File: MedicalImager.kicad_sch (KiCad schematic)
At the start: 0 parts

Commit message: finished SOM 5V power, migrated altium stuff, finished pin study, added USB PHY (revise HS capability)
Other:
- added sheet Interface (Interface.kicad_sch)
- note added: "TODO: - Complete power circuit (one instance of 4A & 1A modules) - Set up power sequencing stuff - Complete the AD8285's part (duplicated in all replicas) - Figure out power requirements (which banks, USB?, etc.) - Link peripherals in K26 to components - Set up circuit protection measures - Add an SD card (if not found on SOM)"
- note removed: "TODO: - Complete pinout stidy of k26 - Migrate progress in altium to here (TX dcaps)"
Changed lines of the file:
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@@
 	(generator_version "10.0")
 	(paper "A4")
-	(text "TODO:\n- Complete pinout stidy of k26\n- Migrate progress in altium to here (TX dcaps)"
+	(text "TODO:\n- Complete power circuit (one instance of 4A & 1A modules)\n- Set up power sequencing stuff\n- Complete the AD8285's part (duplicated in all replicas)\n- Figure out power requirements (which banks, USB?, etc.)\n- Link peripherals in K26 to components\n- Set up circuit protection measures\n- Add an SD card (if not found on SOM)"
 		(exclude_from_sim no)
-		(at 140.716 142.24 0)
+		(at 30.988 149.352 0)
 		(effects
 			(font
@@
 				(bold yes)
 			)
+			(justify left)
 		)
+	)
+	(sheet
+		(at 203.2 88.9)
+		(size 25.4 25.4)
+		(exclude_from_sim no)
+		(in_bom yes)
+		(on_board yes)
+		(dnp no)
+		(fields_autoplaced yes)
+		(stroke
+			(width 0.1524)
+			(type solid)
+		)
+		(fill
+			(color 0 0 0 0)
+		)
+		(property "Sheetname" "Interface"
+			(at 203.2 88.1884 0)
+			(show_name no)
+			(do_not_autoplace no)
+			(effects
+				(font
+					(size 1.27 1.27)
+				)
+				(justify left bottom)
+			)
+		)
+		(property "Sheetfile" "Interface.kicad_sch"
+			(at 203.2 114.8846 0)
+			(show_name no)
+			(do_not_autoplace no)
+			(effects
+				(font
+					(size 1.27 1.27)
+				)
+				(justify left top)
+			)
+		)
+		(instances
+			(project "MedicalImager"
+				(path "/99848109-7be9-4113-bc9c-faf6c2acfe0b"
+					(page "10")
+				)
+			)
+		)

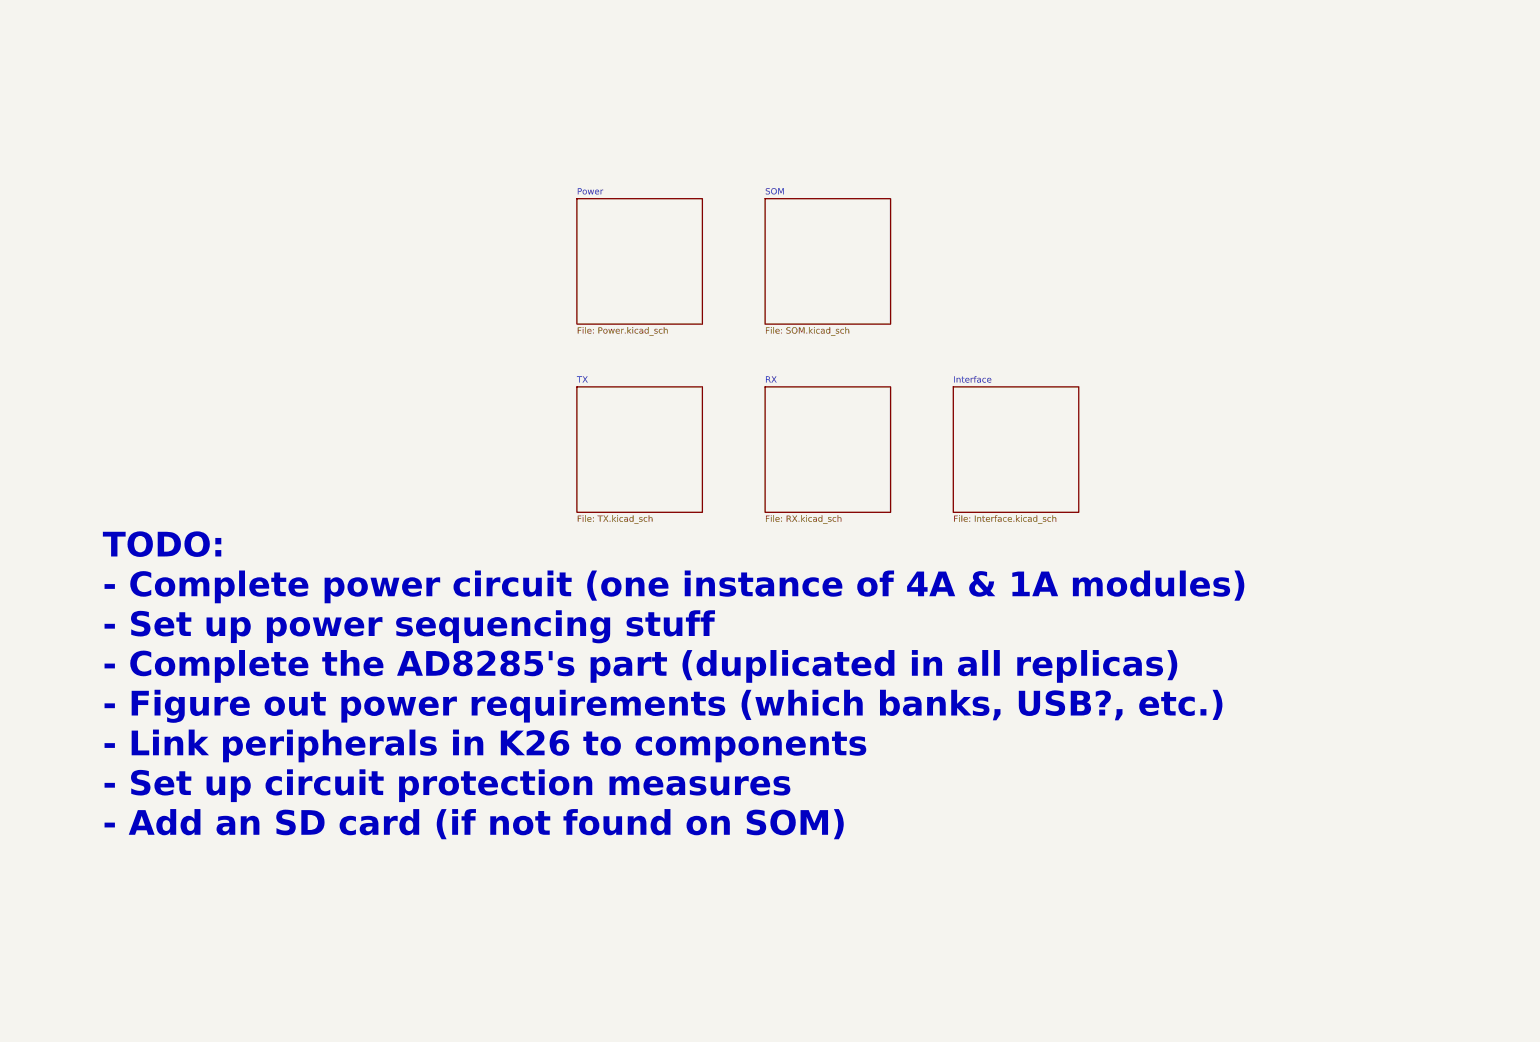
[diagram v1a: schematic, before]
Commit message: finished HV rails (revise, ai), added LDO instances, ready to bind & supply
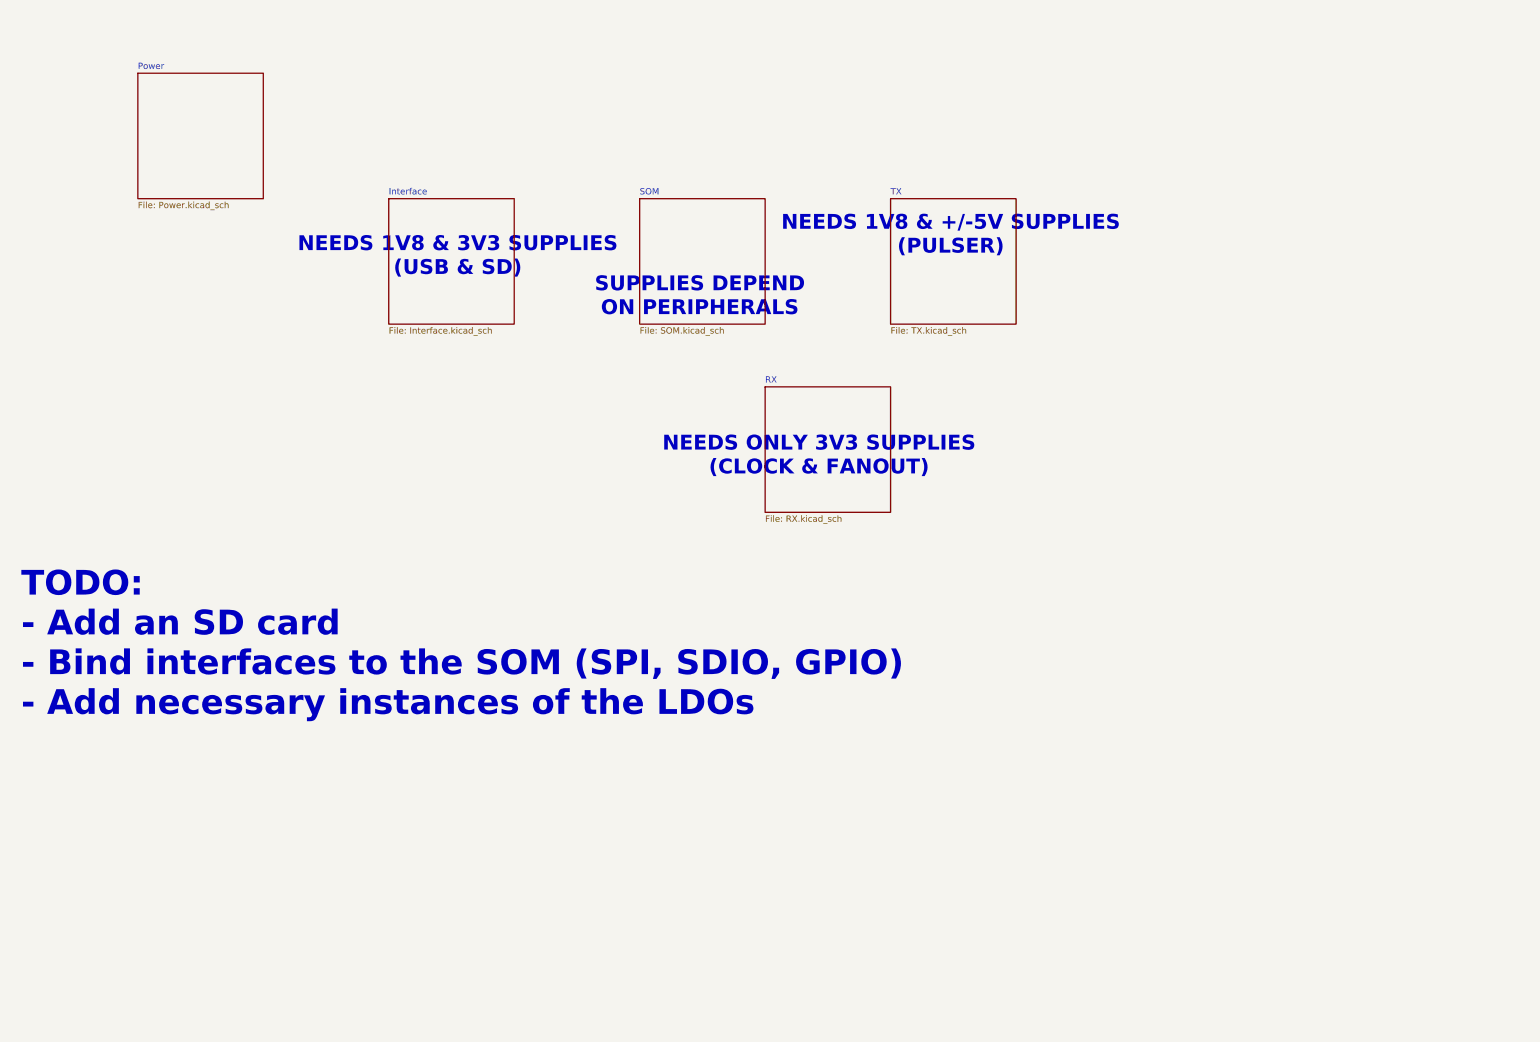
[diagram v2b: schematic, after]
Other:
- note added: "NEEDS 1V8 & +/-5V SUPPLIES (PULSER)"
- note added: "NEEDS 1V8 & 3V3 SUPPLIES (USB & SD)"
- note added: "NEEDS ONLY 3V3 SUPPLIES (CLOCK & FANOUT)"
- note added: "SUPPLIES DEPEND ON PERIPHERALS"
- note added: "TODO: - Add an SD card - Bind interfaces to the SOM (SPI, SDIO, GPIO) - Add necessary instances of the LDOs"
- note removed: "TODO: - Complete power circuit (one instance of 4A & 1A modules) - Set up power sequencing stuff - Complete the AD8285's part (duplicated in all replicas) - Figure out power requirements (which banks, USB?, etc.) - Link peripherals in K26 to components - Set up circuit protection measures - Add an SD card (if not found on SOM)"
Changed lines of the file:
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@@
 	(generator_version "10.0")
 	(paper "A4")
-	(text "TODO:\n- Complete power circuit (one instance of 4A & 1A modules)\n- Set up power sequencing stuff\n- Complete the AD8285's part (duplicated in all replicas)\n- Figure out power requirements (which banks, USB?, etc.)\n- Link peripherals in K26 to components\n- Set up circuit protection measures\n- Add an SD card (if not found on SOM)"
-		(exclude_from_sim no)
-		(at 30.988 149.352 0)
+	(text "TODO:\n- Add an SD card\n- Bind interfaces to the SOM (SPI, SDIO, GPIO)\n- Add necessary instances of the LDOs"
+		(exclude_from_sim no)
+		(at 14.478 140.97 0)
 		(effects
 			(font
@@
 		)
 	)
-	(sheet
-		(at 203.2 88.9)
+	(text "NEEDS 1V8 & +/-5V SUPPLIES\n(PULSER)"
+		(exclude_from_sim no)
+		(at 202.692 58.166 0)
+		(effects
+			(font
+				(size 3 3)
+				(thickness 0.6)
+				(bold yes)
+			)
+		)
+	)
+	(text "SUPPLIES DEPEND\nON PERIPHERALS"
+		(exclude_from_sim no)
+		(at 151.892 70.612 0)
+		(effects
+			(font
+				(size 3 3)
+				(thickness 0.6)
+				(bold yes)
+			)
+		)
+	)
+	(text "NEEDS ONLY 3V3 SUPPLIES\n(CLOCK & FANOUT)"
+		(exclude_from_sim no)
+		(at 176.022 102.87 0)
+		(effects
+			(font
+				(size 3 3)
+				(thickness 0.6)
+				(bold yes)
+			)
+		)
+	)
+	(text "NEEDS 1V8 & 3V3 SUPPLIES\n(USB & SD)"
+		(exclude_from_sim no)
+		(at 102.87 62.484 0)
+		(effects
+			(font
+				(size 3 3)
+				(thickness 0.6)
+				(bold yes)
+			)
+		)
+	)
+	(sheet
+		(at 88.9 50.8)
 		(size 25.4 25.4)
 		(exclude_from_sim no)
@@
 		)
 		(property "Sheetname" "Interface"
-			(at 203.2 88.1884 0)
+			(at 88.9 50.0884 0)
 			(show_name no)
 			(do_not_autoplace no)
@@
 		)
 		(property "Sheetfile" "Interface.kicad_sch"
-			(at 203.2 114.8846 0)
+			(at 88.9 76.7846 0)
 			(show_name no)
 			(do_not_autoplace no)
@@
 	)
 	(sheet
-		(at 165.1 50.8)
+		(at 139.7 50.8)
 		(size 25.4 25.4)
 		(exclude_from_sim no)
@@
 		)
 		(property "Sheetname" "SOM"
-			(at 165.1 50.0884 0)
+			(at 139.7 50.0884 0)
 			(show_name no)
 			(do_not_autoplace no)
@@
 		)
 		(property "Sheetfile" "SOM.kicad_sch"
-			(at 165.1 76.7846 0)
+			(at 139.7 76.7846 0)
 			(show_name no)
 			(do_not_autoplace no)
@@
 	)
 	(sheet
-		(at 127 88.9)
+		(at 190.5 50.8)
 		(size 25.4 25.4)
 		(exclude_from_sim no)
@@
 		)
 		(property "Sheetname" "TX"
-			(at 127 88.1884 0)
+			(at 190.5 50.0884 0)
 			(show_name no)
 			(do_not_autoplace no)
@@
 		)
 		(property "Sheetfile" "TX.kicad_sch"
-			(at 127 114.8846 0)
+			(at 190.5 76.7846 0)
 			(show_name no)
 			(do_not_autoplace no)
@@
 	)
 	(sheet
-		(at 127 50.8)
+		(at 38.1 25.4)
 		(size 25.4 25.4)
 		(exclude_from_sim no)
@@
 		)
 		(property "Sheetname" "Power"
-			(at 127 50.0884 0)
+			(at 38.1 24.6884 0)
 			(show_name no)
 			(do_not_autoplace no)
@@
 		)
 		(property "Sheetfile" "Power.kicad_sch"
-			(at 127 76.7846 0)
-			(show_name no)
-			(do_not_autoplace no)
+			(at 38.1 51.3846 0)
+			(show_name no)
+			(do_not_autoplace no)

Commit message: added USB (needs revision), fixed medium voltage rail
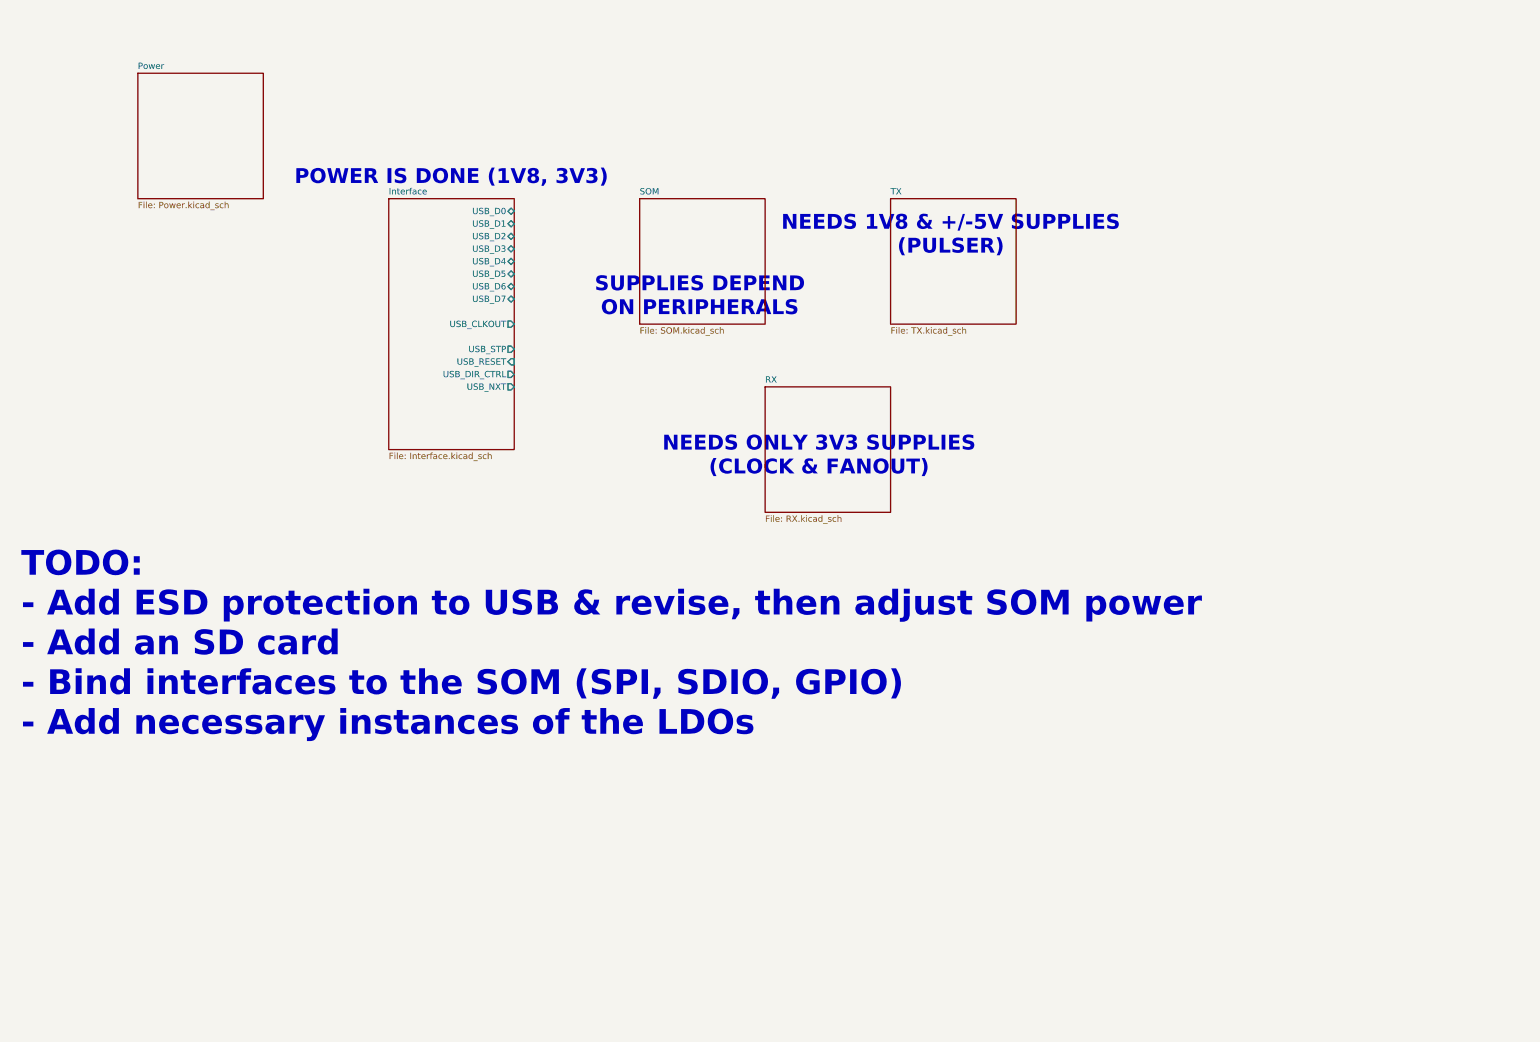
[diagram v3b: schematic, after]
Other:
- sheet Interface ports: added USB_CLKOUT, USB_D0, USB_D1, USB_D2, USB_D3, USB_D4, USB_D5, USB_D6, USB_D7, USB_DIR_CTRL, USB_NXT, USB_RESET, USB_STP; removed none
- note added: "POWER IS DONE (1V8, 3V3)"
- note added: "TODO: - Add ESD protection to USB & revise, then adjust SOM power - Add an SD card - Bind interfaces to the SOM (SPI, SDIO, GPIO) - Add necessary instances of the LDOs"
- note removed: "NEEDS 1V8 & 3V3 SUPPLIES (USB & SD)"
- note removed: "TODO: - Add an SD card - Bind interfaces to the SOM (SPI, SDIO, GPIO) - Add necessary instances of the LDOs"
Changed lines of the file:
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@@
 	(generator_version "10.0")
 	(paper "A4")
-	(text "TODO:\n- Add an SD card\n- Bind interfaces to the SOM (SPI, SDIO, GPIO)\n- Add necessary instances of the LDOs"
+	(text "TODO:\n- Add ESD protection to USB & revise, then adjust SOM power\n- Add an SD card\n- Bind interfaces to the SOM (SPI, SDIO, GPIO)\n- Add necessary instances of the LDOs"
 		(exclude_from_sim no)
 		(at 14.478 140.97 0)
@@
 		)
 	)
+	(text "POWER IS DONE (1V8, 3V3)"
+		(exclude_from_sim no)
+		(at 101.6 46.482 0)
+		(effects
+			(font
+				(size 3 3)
+				(thickness 0.6)
+				(bold yes)
+			)
+		)
+	)
 	(text "NEEDS ONLY 3V3 SUPPLIES\n(CLOCK & FANOUT)"
 		(exclude_from_sim no)
 		(at 176.022 102.87 0)
-		(effects
-			(font
-				(size 3 3)
-				(thickness 0.6)
-				(bold yes)
-			)
-		)
-	)
-	(text "NEEDS 1V8 & 3V3 SUPPLIES\n(USB & SD)"
-		(exclude_from_sim no)
-		(at 102.87 62.484 0)
 		(effects
 			(font
@@
 	(sheet
 		(at 88.9 50.8)
-		(size 25.4 25.4)
+		(size 25.4 50.8)
 		(exclude_from_sim no)
 		(in_bom yes)
@@
 		)
 		(property "Sheetfile" "Interface.kicad_sch"
-			(at 88.9 76.7846 0)
+			(at 88.9 102.1846 0)
 			(show_name no)
 			(do_not_autoplace no)
@@
 			)
 		)
+		(pin "USB_D7" bidirectional
+			(at 114.3 71.12 0)
+			(effects
+				(font
+					(size 1.27 1.27)
+				)
+				(justify right)
+			)
+		)
+		(pin "USB_D0" bidirectional
+			(at 114.3 53.34 0)
+			(effects
+				(font
+					(size 1.27 1.27)
+				)
+				(justify right)
+			)
+		)
+		(pin "USB_CLKOUT" output
+			(at 114.3 76.2 0)
+			(effects
+				(font
+					(size 1.27 1.27)
+				)
+				(justify right)
+			)
+		)
+		(pin "USB_D4" bidirectional
+			(at 114.3 63.5 0)
+			(effects
+				(font
+					(size 1.27 1.27)
+				)
+				(justify right)
+			)
+		)
+		(pin "USB_D3" bidirectional
+			(at 114.3 60.96 0)
+			(effects
+				(font
+					(size 1.27 1.27)
+				)
+				(justify right)
+			)
+		)
+		(pin "USB_D1" bidirectional
+			(at 114.3 55.88 0)
+			(effects
+				(font
+					(size 1.27 1.27)
+				)
+				(justify right)
+			)
+		)
+		(pin "USB_STP" output
+			(at 114.3 81.28 0)
+			(effects
+				(font
+					(size 1.27 1.27)
+				)
+				(justify right)
+			)
+		)
+		(pin "USB_RESET" input
+			(at 114.3 83.82 0)
+			(effects
+				(font
+					(size 1.27 1.27)
+				)
+				(justify right)
+			)
+		)
+		(pin "USB_D6" bidirectional
+			(at 114.3 68.58 0)
+			(effects
+				(font
+					(size 1.27 1.27)
+				)
+				(justify right)
+			)
+		)
+		(pin "USB_DIR_CTRL" output
+			(at 114.3 86.36 0)
+			(effects
+				(font
+					(size 1.27 1.27)
+				)
+				(justify right)
+			)
+		)
+		(pin "USB_NXT" output
+			(at 114.3 88.9 0)
+			(effects
+				(font
+					(size 1.27 1.27)
+				)
+				(justify right)
+			)
+		)
+		(pin "USB_D5" bidirectional
+			(at 114.3 66.04 0)
+			(effects
+				(font
+					(size 1.27 1.27)
+				)
+				(justify right)
+			)
+		)
+		(pin "USB_D2" bidirectional
+			(at 114.3 58.42 0)
+			(effects
+				(font
+					(size 1.27 1.27)
+				)
+				(justify right)
+			)
+		)

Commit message: almost finished, phew! just dd +/- 5v rails, connect the SDIO & power enable pins and figure out the rest of the clocking chain
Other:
- sheet Interface ports: added SD_CLK, SD_CMD, SD_DAT0, SD_DAT1, SD_DAT2, SD_DAT3, SD_DETECT; removed none
- sheet Power ports: added 100V_EN, 50V_EN, AFE1_1V8_EN, AFE1_3V3_EN, AFE2_1V8_EN, AFE2_3V3_EN, AFE3_1V8_EN, AFE3_3V3_EN, AFE4_1V8_EN, AFE4_3V3_EN, CLK_PWR_EN, IM_5V_PG, PULSER_1V8_EN, SOM_5V_PG, SOM_PL_PWR_EN, USB_1V8_EN; removed none
- sheet RX ports: added AFE1_AUX, AFE1_CSn, AFE1_DSYNC, AFE1_MUXA, AFE2_AUX, AFE2_CSn, AFE2_DSYNC, AFE2_MUXA, AFE3_AUX, AFE3_CSn, AFE3_DSYNC, AFE3_MUXA, AFE4_AUX, AFE4_CSn, AFE4_DSYNC, AFE4_MUXA, AFE_OUTPUTS[0..47], AFE_SCLK, AFE_SDIO, SOM_SYNC_CLK_N, SOM_SYNC_CLK_P, TR_OUT[0..15], TX_BF_CLK_N, TX_BF_CLK_P; removed none
- sheet SOM ports: added 100V_EN, 50V_EN, AFE1_1V8_EN, AFE1_3V3_EN, AFE1_AUX, AFE1_CSn, AFE1_DSYNC, AFE1_MUXA, AFE2_1V8_EN, AFE2_3V3_EN, AFE2_AUX, AFE2_CSn, AFE2_DSYNC, AFE2_MUXA, AFE3_1V8_EN, AFE3_3V3_EN, AFE3_AUX, AFE3_CSn, AFE3_DSYNC, AFE3_MUXA, AFE4_1V8_EN, AFE4_3V3_EN, AFE4_AUX, AFE4_CSn, AFE4_DSYNC, AFE4_MUXA, AFE_OUTPUTS[0..47], AFE_SCLK, AFE_SDIO, CLK_PWR_EN, IM_5V_PG, PULSER_1V8_EN, PULSER_BF_SYNC_CLK_N, PULSER_BF_SYNC_CLK_P, PULSER_CRC_ERR, PULSER_RESET, PULSER_SPI_CLK_N, PULSER_SPI_CLK_P, PULSER_SPI_CRC_EN, PULSER_SPI_CS0, PULSER_SPI_CS1, PULSER_SPI_D0_N, PULSER_SPI_D0_P, PULSER_SPI_D1_N, PULSER_SPI_D1_P, PULSER_SPI_MODE, PULSER_SPI_SDOUT, PULSER_SPI_SE_N, PULSER_SPI_SE_P, PULSER_TSHUT, PULSER_TXRX, PULSER_WAKEUP, SD_CLK, SD_CMD, SD_DAT0, SD_DAT1, SD_DAT2, SD_DAT3, SD_DETECT, SOM_5V_PG, SOM_PL_PWR_EN, SOM_PS_PWR_EN, SOM_SYNC_CLK_N, SOM_SYNC_CLK_P, USB_1V8_EN, USB_CLKOUT, USB_D0, USB_D1, USB_D2, USB_D3, USB_D4, USB_D5, USB_D6, USB_D7, USB_DIR_CTRL, USB_NXT, USB_STP; removed none
- sheet TX ports: added PULSER_BF_CLK_N, PULSER_BF_CLK_P, PULSER_BF_SYNC_CLK_N, PULSER_BF_SYNC_CLK_P, PULSER_CRC_ERR, PULSER_OUT[0..15], PULSER_RESET, PULSER_SPI_CLK_N, PULSER_SPI_CLK_P, PULSER_SPI_CRC_EN, PULSER_SPI_CS0, PULSER_SPI_CS1, PULSER_SPI_D0_N, PULSER_SPI_D0_P, PULSER_SPI_D1_N, PULSER_SPI_D1_P, PULSER_SPI_MODE, PULSER_SPI_SDOUT, PULSER_SPI_SE_N, PULSER_SPI_SE_P, PULSER_TSHUT, PULSER_TXRX, PULSER_WAKEUP, TR_OUT[0..15]; removed none
- note added: "NEEDS +/-5V SUPPLIES (PULSER)"
- note added: "TODO: - Complete missing interfaces (SDIO & clocking) - Check un-supplied rails (including -5V)"
- note removed: "NEEDS 1V8 & +/-5V SUPPLIES (PULSER)"
- note removed: "NEEDS ONLY 3V3 SUPPLIES (CLOCK & FANOUT)"
- note removed: "POWER IS DONE (1V8, 3V3)"
- note removed: "TODO: - Add ESD protection to USB & revise, then adjust SOM power - Add an SD card - Bind interfaces to the SOM (SPI, SDIO, GPIO) - Add necessary instances of the LDOs"

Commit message: DONE! hust needs a final revision, checking termination throughout the circuit and verifying the signal chain
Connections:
- no-connect marks 0 -> 1
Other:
- sheet Power ports: added -5V_EN, IM_5V_EN, SD_3V3_EN; removed none
- sheet SOM ports: added -5V_EN, IM_5V_EN, SD_3V3_EN; removed none
- note added: "- FINALIZE CLOCKING CONNECTIONS AND TERMINATION THROUGHOUT THE CIRCUIT - VERIFY SIGNAL CHAIN COMPATIBILITY"
- note removed: "NEEDS +/-5V SUPPLIES (PULSER)"
- note removed: "SUPPLIES DEPEND ON PERIPHERALS"
- note removed: "TODO: - Complete missing interfaces (SDIO & clocking) - Check un-supplied rails (including -5V)"
